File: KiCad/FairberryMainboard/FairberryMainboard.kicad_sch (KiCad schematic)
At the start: 19 parts, among them J1 USB_Header, J2 Conn_02x03_Odd_Even, J3 Conn_02x02_Odd_Even, J4 Conn_01x02, U1 ATmega32U4-MU, U2 BBQ10KBD, Y1 Crystal_GND24

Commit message: Kicad files for mainboard v0.2.0
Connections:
- net at U1.1 (PE6): now also U2.8 (ROW2)
- net at U1.38 (PF5): now also J3.4 (Pin_4); no longer U2.8 (ROW2)
- net at U1.39 (PF4): now also J3.3 (Pin_3); no longer J3.4 (Pin_4)
- net at C3.1, U1.42 (AREF): no longer J3.3 (Pin_3)
- no-connect marks 4 -> 3
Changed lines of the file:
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@@
   (junction (at 220.98 91.44) (diameter 0) (color 0 0 0 0)
   )
-  (no_connect (at 152.4 113.03))
   (no_connect (at 152.4 57.15))
   (no_connect (at 220.98 60.96))
   (no_connect (at 220.98 78.74))
+  (wire (pts (xy 275.59 125.73) (xy 275.59 154.94))
+    (stroke (width 0) (type default) (color 0 0 0 0))
+  )
+  (wire (pts (xy 275.59 154.94) (xy 266.7 154.94))
+    (stroke (width 0) (type default) (color 0 0 0 0))
+  )
   (wire (pts (xy 110.49 57.15) (xy 110.49 39.37))
     (stroke (width 0) (type default) (color 0 0 0 0))
@@
     (stroke (width 0) (type default) (color 0 0 0 0))
   )
-  (wire (pts (xy 167.64 148.59) (xy 167.64 157.48))
-    (stroke (width 0) (type default) (color 0 0 0 0))
-  )
   (wire (pts (xy 100.33 68.58) (xy 100.33 64.77))
     (stroke (width 0) (type default) (color 0 0 0 0))
@@
     (stroke (width 0) (type default) (color 0 0 0 0))
   )
+  (wire (pts (xy 267.97 78.74) (xy 267.97 113.03))
+    (stroke (width 0) (type default) (color 0 0 0 0))
+  )
   (wire (pts (xy 237.49 147.32) (xy 242.57 147.32))
     (stroke (width 0) (type default) (color 0 0 0 0))
@@
     (stroke (width 0) (type default) (color 0 0 0 0))
   )
-  (wire (pts (xy 267.97 78.74) (xy 267.97 125.73))
-    (stroke (width 0) (type default) (color 0 0 0 0))
-  )
   (wire (pts (xy 152.4 105.41) (xy 269.24 105.41))
     (stroke (width 0) (type default) (color 0 0 0 0))
@@
     (stroke (width 0) (type default) (color 0 0 0 0))
   )
-  (wire (pts (xy 154.94 107.95) (xy 177.8 107.95))
-    (stroke (width 0) (type default) (color 0 0 0 0))
-  )
   (wire (pts (xy 251.46 60.96) (xy 274.32 60.96))
     (stroke (width 0) (type default) (color 0 0 0 0))
@@
     (stroke (width 0) (type default) (color 0 0 0 0))
   )
+  (wire (pts (xy 152.4 92.71) (xy 177.8 92.71))
+    (stroke (width 0) (type default) (color 0 0 0 0))
+  )
   (wire (pts (xy 271.78 66.04) (xy 271.78 95.25))
     (stroke (width 0) (type default) (color 0 0 0 0))
@@
     (stroke (width 0) (type default) (color 0 0 0 0))
   )
-  (wire (pts (xy 152.4 92.71) (xy 154.94 92.71))
-    (stroke (width 0) (type default) (color 0 0 0 0))
-  )
   (wire (pts (xy 193.04 72.39) (xy 152.4 72.39))
     (stroke (width 0) (type default) (color 0 0 0 0))
@@
     (stroke (width 0) (type default) (color 0 0 0 0))
   )
-  (wire (pts (xy 251.46 154.94) (xy 254 154.94))
-    (stroke (width 0) (type default) (color 0 0 0 0))
-  )
   (wire (pts (xy 220.98 71.12) (xy 220.98 73.66))
     (stroke (width 0) (type default) (color 0 0 0 0))
   )
-  (wire (pts (xy 167.64 148.59) (xy 87.63 148.59))
-    (stroke (width 0) (type default) (color 0 0 0 0))
-  )
   (wire (pts (xy 205.74 39.37) (xy 205.74 147.32))
     (stroke (width 0) (type default) (color 0 0 0 0))
   )
+  (wire (pts (xy 152.4 113.03) (xy 267.97 113.03))
+    (stroke (width 0) (type default) (color 0 0 0 0))
+  )
   (wire (pts (xy 205.74 147.32) (xy 224.79 147.32))
     (stroke (width 0) (type default) (color 0 0 0 0))
@@
     (stroke (width 0) (type default) (color 0 0 0 0))
   )
+  (wire (pts (xy 254 154.94) (xy 254 158.75))
+    (stroke (width 0) (type default) (color 0 0 0 0))
+  )
   (wire (pts (xy 247.65 139.7) (xy 247.65 134.62))
     (stroke (width 0) (type default) (color 0 0 0 0))
@@
     (stroke (width 0) (type default) (color 0 0 0 0))
   )
-  (wire (pts (xy 154.94 92.71) (xy 154.94 107.95))
-    (stroke (width 0) (type default) (color 0 0 0 0))
-  )
   (wire (pts (xy 201.93 142.24) (xy 224.79 142.24))
     (stroke (width 0) (type default) (color 0 0 0 0))
@@
     (stroke (width 0) (type default) (color 0 0 0 0))
   )
-  (wire (pts (xy 177.8 107.95) (xy 177.8 92.71))
-    (stroke (width 0) (type default) (color 0 0 0 0))
-  )
   (wire (pts (xy 114.3 60.96) (xy 121.92 60.96))
     (stroke (width 0) (type default) (color 0 0 0 0))
@@
     (stroke (width 0) (type default) (color 0 0 0 0))
   )
-  (wire (pts (xy 152.4 125.73) (xy 267.97 125.73))
+  (wire (pts (xy 152.4 125.73) (xy 275.59 125.73))
     (stroke (width 0) (type default) (color 0 0 0 0))
   )
@@
     (stroke (width 0) (type default) (color 0 0 0 0))
   )
-  (wire (pts (xy 167.64 157.48) (xy 251.46 157.48))
-    (stroke (width 0) (type default) (color 0 0 0 0))
-  )
   (wire (pts (xy 110.49 39.37) (xy 205.74 39.37))
     (stroke (width 0) (type default) (color 0 0 0 0))
@@
     (stroke (width 0) (type default) (color 0 0 0 0))
   )
-  (wire (pts (xy 266.7 154.94) (xy 266.7 158.75))
-    (stroke (width 0) (type default) (color 0 0 0 0))
-  )
-  (wire (pts (xy 251.46 157.48) (xy 251.46 154.94))
-    (stroke (width 0) (type default) (color 0 0 0 0))
-  )
   (wire (pts (xy 152.4 64.77) (xy 201.93 64.77))
     (stroke (width 0) (type default) (color 0 0 0 0))
@@
     (stroke (width 0) (type default) (color 0 0 0 0))
   )
-  (wire (pts (xy 198.12 158.75) (xy 266.7 158.75))
-    (stroke (width 0) (type default) (color 0 0 0 0))
-  )
+  (wire (pts (xy 198.12 158.75) (xy 254 158.75))
+    (stroke (width 0) (type default) (color 0 0 0 0))
+  )

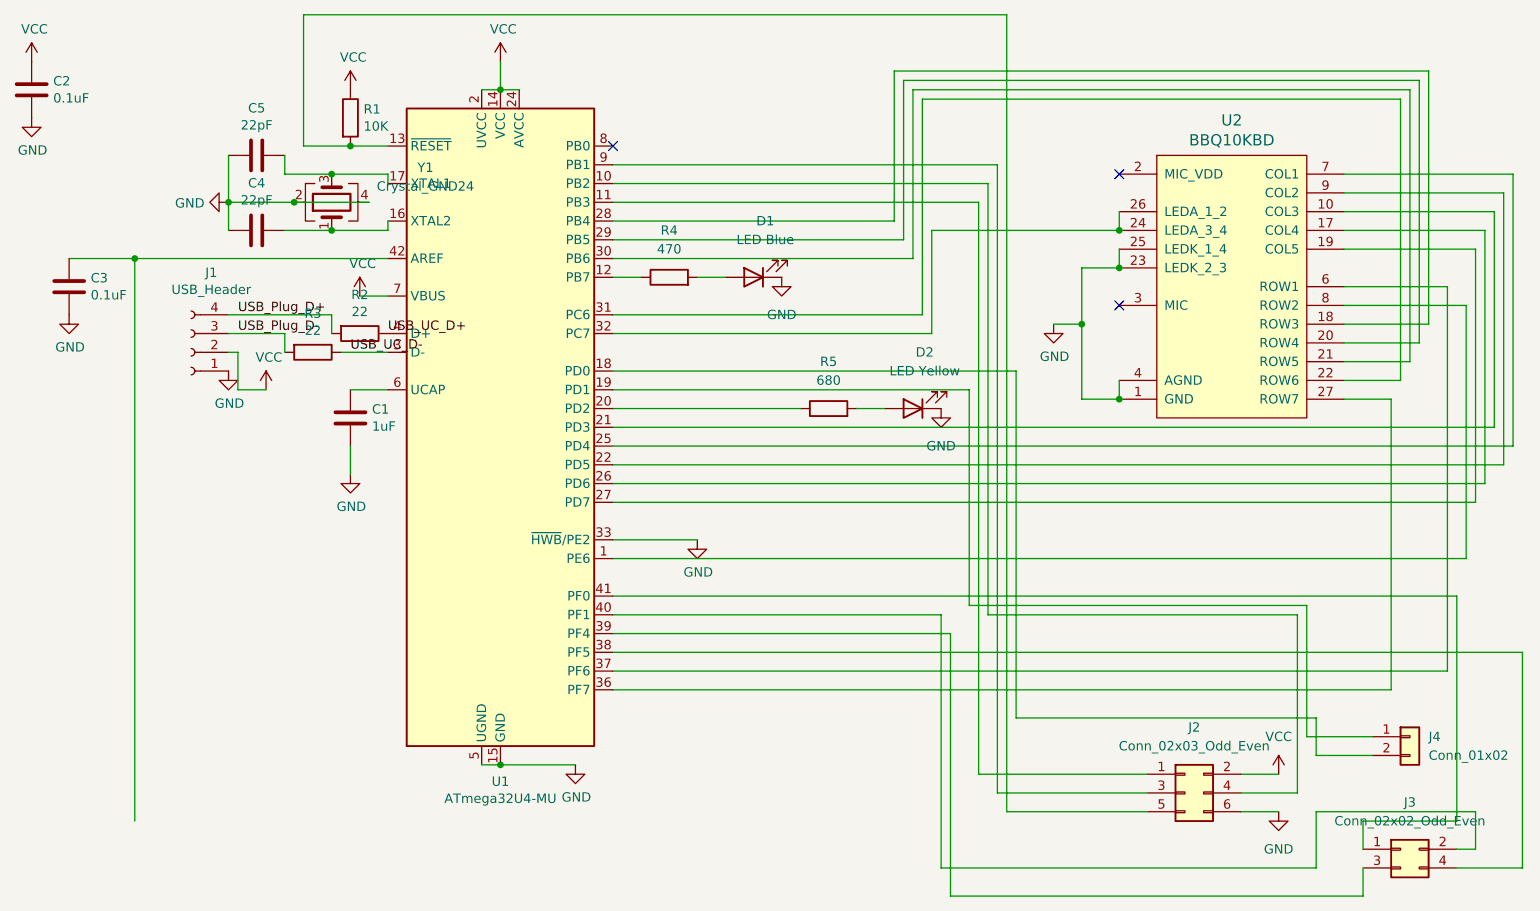
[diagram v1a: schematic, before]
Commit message: Hardware revision v0.3.0 (#16) (#19)
* Split backlight into two zones, removed status LEDs, reduced y size by 1mm

* Made firmware compatible with v0.3.0 (doesn't make use of dual backlight controls yet), refactoring

* Improved Case Generator script, added presets for Fairphone 4 and Samsung Galaxy A54

* Finalisation of v0.3.0 PCB

* License/Version header for firmware

* Removed generated stl
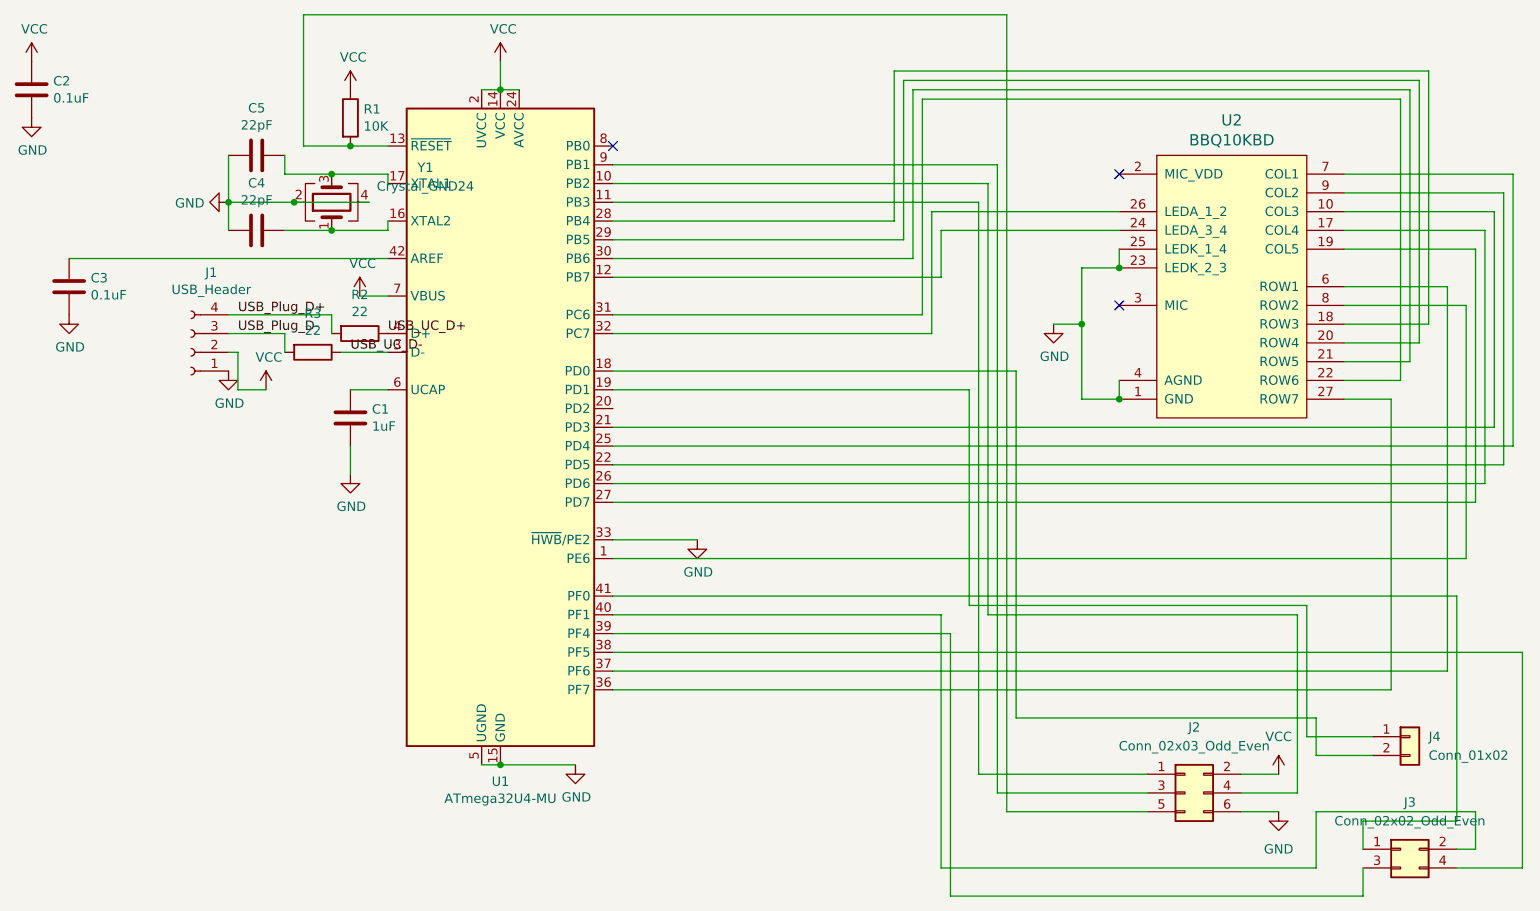
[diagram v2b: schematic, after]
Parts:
- removed D1: LED Blue, LED_SMD:LED_0603_1608Metric, symbol Device:LED
- removed D2: LED Yellow, LED_SMD:LED_0603_1608Metric, symbol Device:LED
- removed R4: 470, Resistor_SMD:R_0402_1005Metric, symbol Device:R
- removed R5: 680, Resistor_SMD:R_0402_1005Metric, symbol Device:R
- J3: footprint Fairberry:TestPoint_Pad_1+3_2.0x3.0mm_slim -> Fairberry:TestPoint_Pad_2+2_Z_2.0x2.0mm
- J4: footprint Fairberry:TestPoint_Pad_1x2_2.0x3.0mm -> Fairberry:TestPoint_Pad_1x2_2.0x3.0mm_Rotated
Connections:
- net at U1.12 (PB7): now also U2.24 (LEDA_3_4)
- net at U1.32 (PC7), U2.26 (LEDA_1_2): no longer U2.24 (LEDA_3_4)
